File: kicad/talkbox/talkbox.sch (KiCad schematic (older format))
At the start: 40 parts, among them J1 AudioJack2, J2 Conn_01x02, J3 AudioJack2, J4 Barrel_Jack_Switch, SW1 SW_SPST, U1 LM386, U2 SW_3PDT, U3 TL071, U4 LT1054xSOIC16, U5 LM7812_TO220, U6 LM7912_TO220

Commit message: Added gitignore
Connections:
- net tone_control_output: now also R1.1, RV3.3
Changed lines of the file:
@@
 	3800 4850 4900 4850
 Wire Wire Line
-	6000 5950 6000 4750
-Wire Wire Line
-	4950 5950 6000 5950
+	6500 5950 6500 4750
+Wire Wire Line
+	4950 5950 6500 5950
 Text GLabel 5100 5350 3    50   Input ~ 0
 VDD
@@
 	5100 4050 5100 4250
 Connection ~ 5100 4250
-Text GLabel 6300 4750 2    50   Input ~ 0
+Text GLabel 6800 4750 2    50   Input ~ 0
 tone_control_output
 Wire Wire Line
-	6300 4750 6000 4750
+	6800 4750 6500 4750
 Wire Notes Line width 39 style dash_dot rgb(132, 132, 132)
 	7700 7050 7700 900
@@
 	13450 2200 13600 2200
 Wire Wire Line
-	5500 4750 6000 4750
-Connection ~ 6000 4750
+	5500 4750 6500 4750
+Connection ~ 6500 4750
 NoConn ~ 6500 9150
 NoConn ~ 6350 7850
@@
 Wire Wire Line
 	2900 8250 2900 8350
+Wire Wire Line
+	6000 1900 6500 1900
+Connection ~ 6000 1900
+Wire Wire Line
+	6500 1900 6500 4750
 $EndSCHEMATC

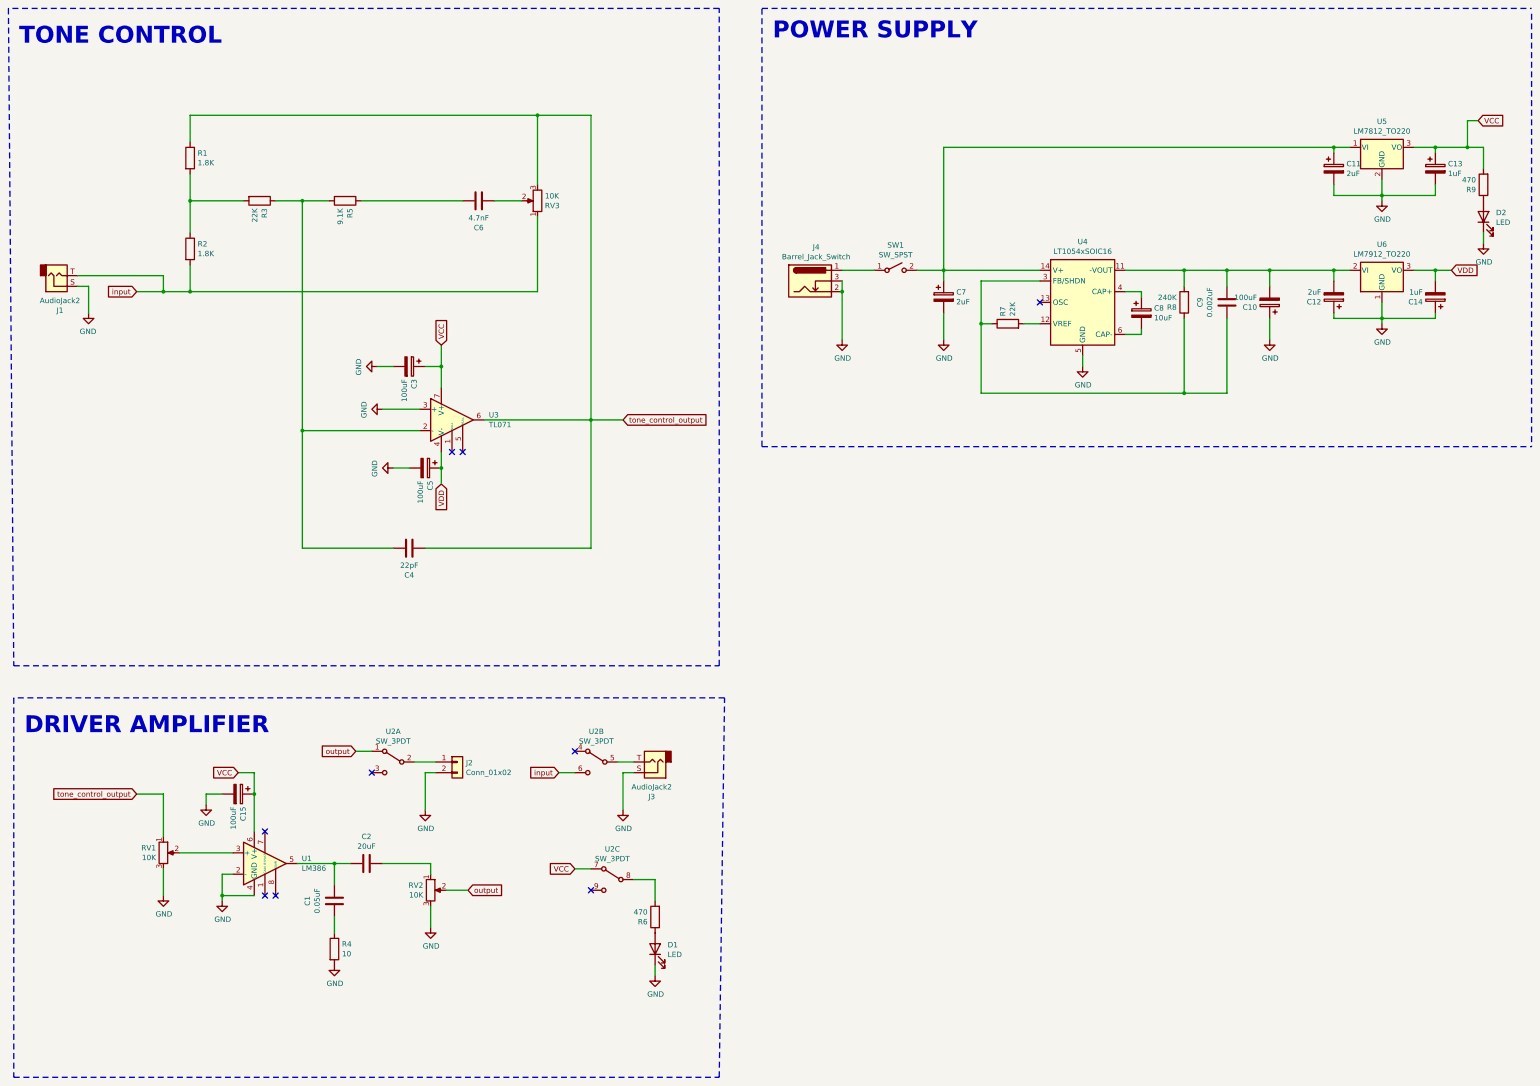
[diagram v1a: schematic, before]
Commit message: Added tl072 and preamp stage
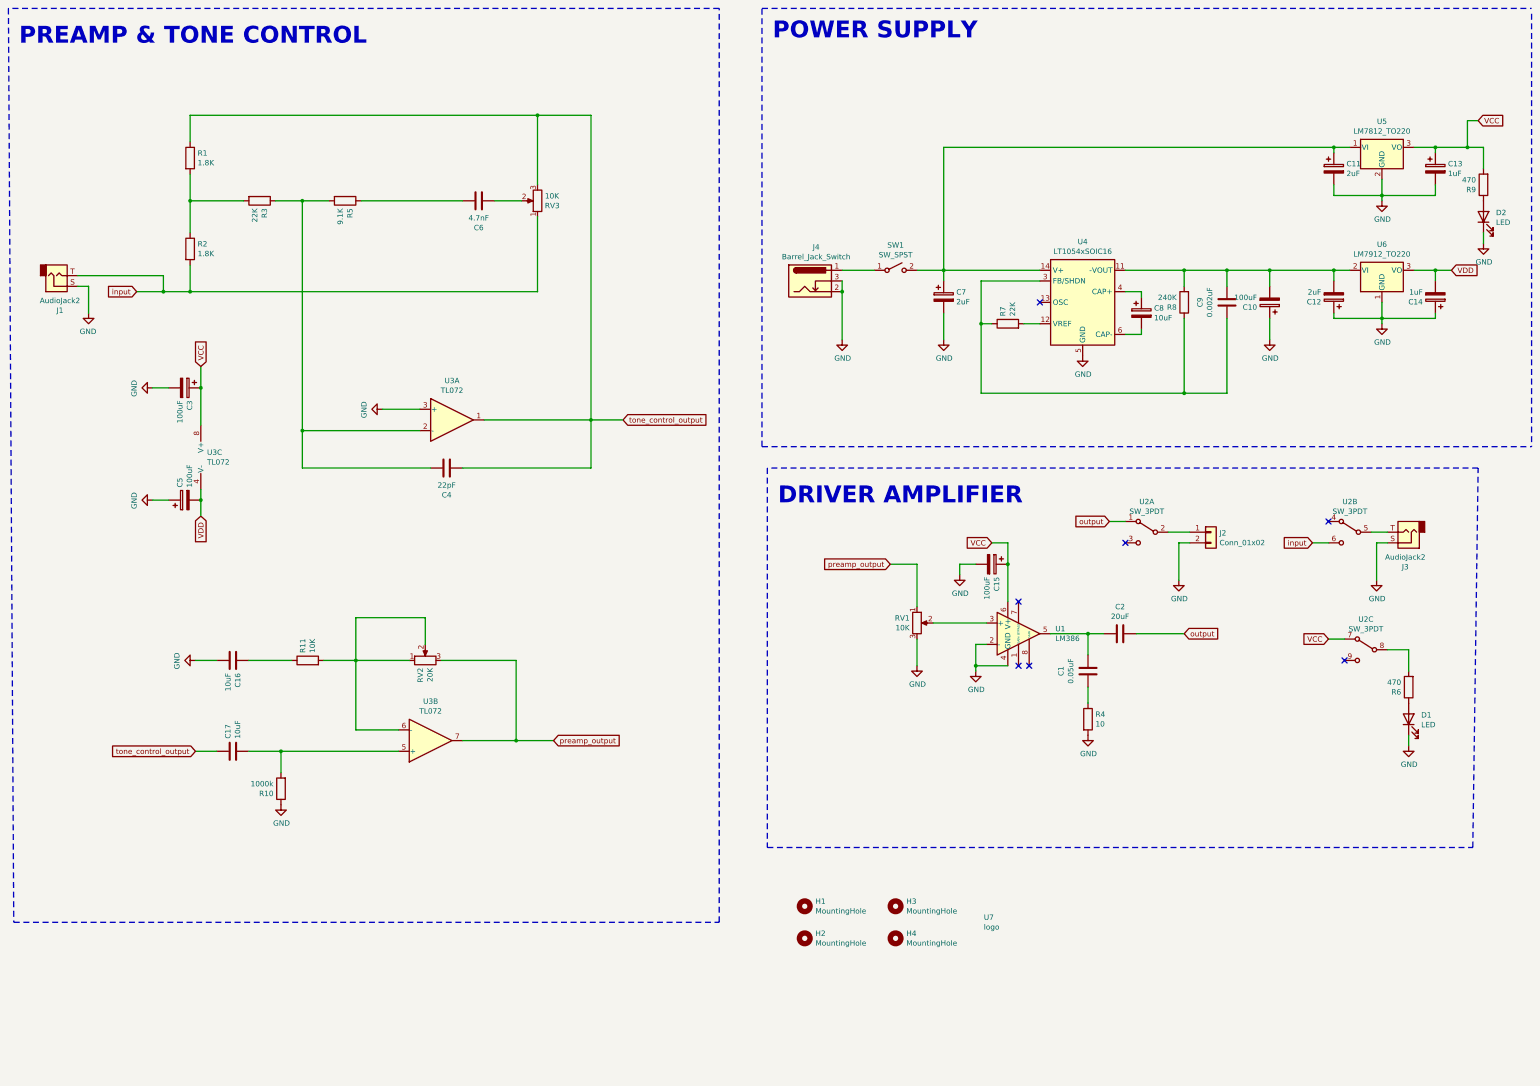
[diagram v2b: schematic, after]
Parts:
- removed U3: TL071, Package_SO:SOIC-8_3.9x4.9mm_P1.27mm, symbol Amplifier_Operational:TL071
- added C16, C17: 10uF, Capacitor_SMD:C_0603_1608Metric, symbol Device:C
- added H1, H2, H3, H4: MountingHole, MountingHole:MountingHole_3mm, symbol Mechanical:MountingHole
- added R10: 1000k, Resistor_SMD:R_0603_1608Metric, symbol Device:R
- added R11: 10K, Resistor_SMD:R_0603_1608Metric, symbol Device:R
- added U3: TL072, Package_SO:SOIC-8_3.9x4.9mm_P1.27mm, symbol Amplifier_Operational:TL072
- added U7: logo, imgs:ratatech_bitmap_10x2.8mm, symbol logo:logo
- RV2: value 10K -> 20K
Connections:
- net GND: now also C5.1, C16.2, R10.1, U3.3 (+); no longer C5.2, RV2.3
- net VCC: now also U3.8 (V+)
- net VDD: now also C5.2, U3.4 (V-); no longer C5.1
- net output: now also C2.1; no longer RV2.2
- net tone_control_output: now also C17.1, U3.1; no longer RV1.1
- net at C4.1, R3.1, R5.2: now also U3.2 (-)
- net at RV2.1: now also RV2.2, R11.2, U3.6 (-); no longer C2.1
- new net: C17.2, R10.2, U3.5 (+)
- new net: C16.1, R11.1
- new net preamp_output: RV1.1, RV2.3, U3.7
- no-connect marks 9 -> 7
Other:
- note added: "PREAMP & TONE CONTROL"
- note removed: "TONE CONTROL"
- moved on the sheet: C1, C15, C2, C3, C4, C5, D1, J2, J3, R4, R6, RV1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

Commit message: Removed lm386 based power amplifier and adapted tone control
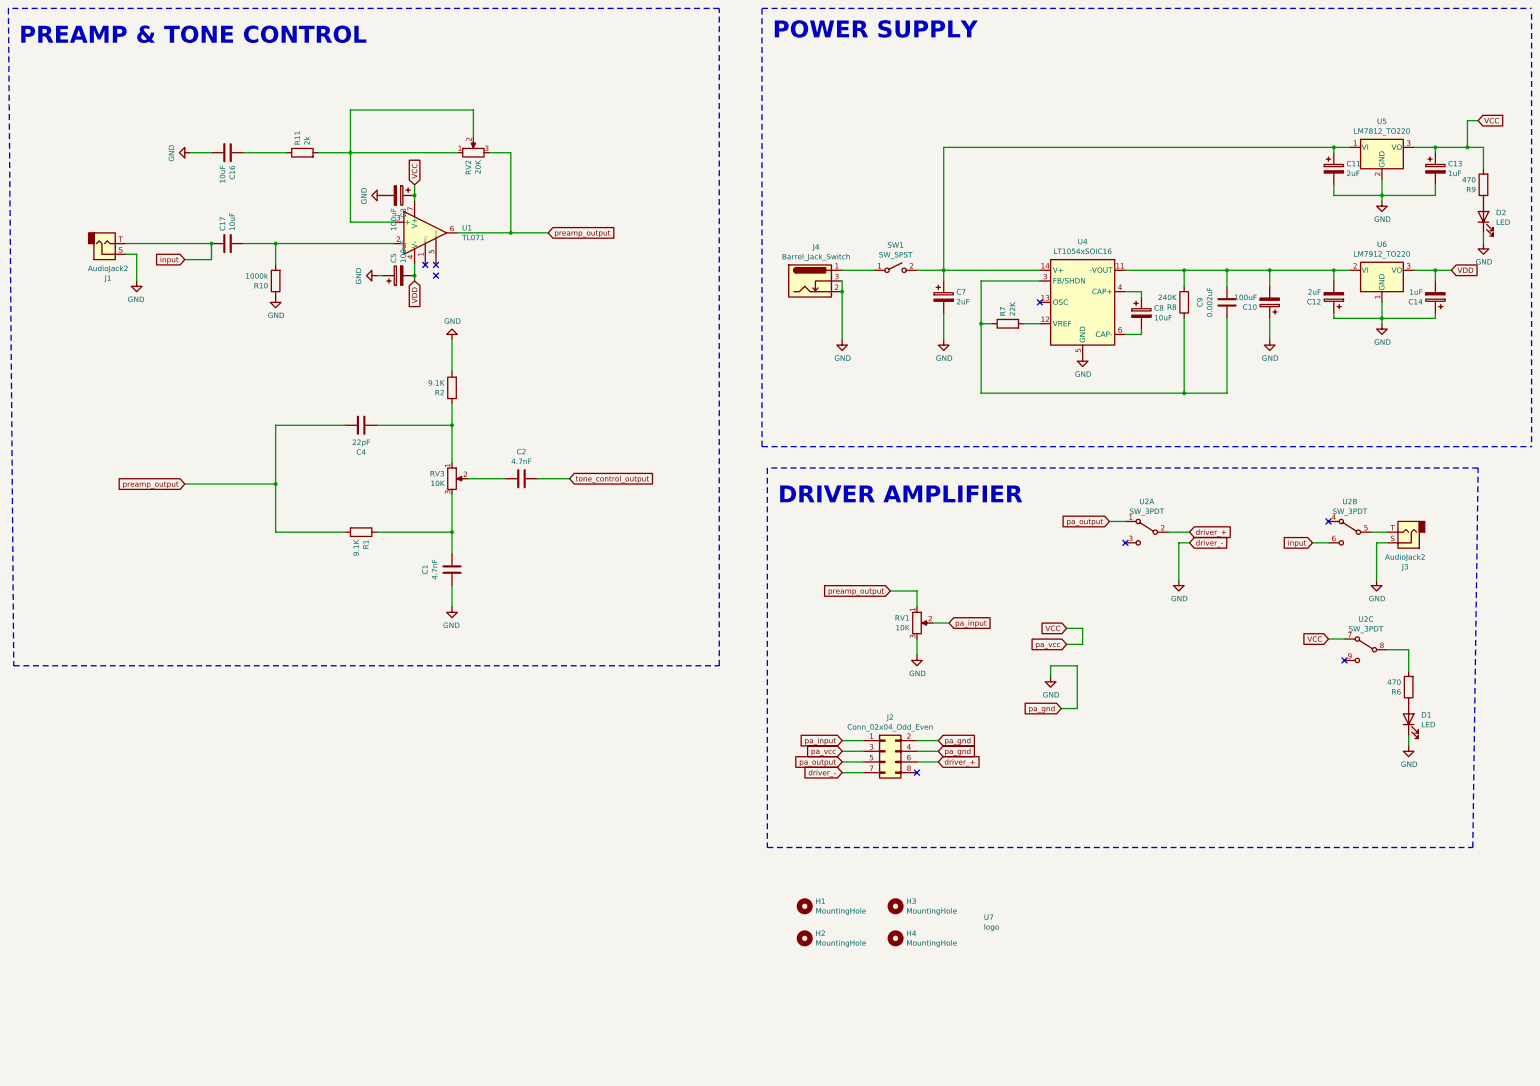
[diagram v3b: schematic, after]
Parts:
- removed C15: 100uF, Capacitor_SMD:CP_Elec_5x5.3, symbol Device:CP
- removed C6: 4.7nF, Capacitor_SMD:C_0603_1608Metric, symbol Device:C
- removed J2: Conn_01x02, Connector_JST:JST_EH_S2B-EH_1x02_P2.50mm_Horizontal, symbol Connector_Generic:Conn_01x02
- removed R3: 22K, Resistor_SMD:R_0603_1608Metric, symbol Device:R
- removed R4: 10, Resistor_SMD:R_0603_1608Metric, symbol Device:R
- removed R5: 9.1K, Resistor_SMD:R_0603_1608Metric, symbol Device:R
- removed U1: LM386, Package_SO:SOIC-8_3.9x4.9mm_P1.27mm, symbol Amplifier_Audio:LM386
- removed U3: TL072, Package_SO:SOIC-8_3.9x4.9mm_P1.27mm, symbol Amplifier_Operational:TL072
- added J2: Conn_02x04_Odd_Even, Connector_PinHeader_2.54mm:PinHeader_2x04_P2.54mm_Vertical, symbol Connector_Generic:Conn_02x04_Odd_Even
- added U1: TL071, Package_SO:SOIC-8_3.9x4.9mm_P1.27mm, symbol Amplifier_Operational:TL071
- C1: value 0.05uF -> 4.7nF
- C2: value 20uF -> 4.7nF; footprint Capacitor_SMD:CP_Elec_5x5.3 -> Capacitor_SMD:C_0603_1608Metric
- R1, R2: value 1.8K -> 9.1K
- R11: value 10K -> 2k
- U2: footprint Stompbox_Switch:SW_Stompbox_3PDT_redux -> Connector_PinHeader_2.54mm:PinHeader_2x05_P2.54mm_Vertical
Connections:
- net GND: now also C1.2, R2.2, J2.2 (Pin_2), J2.4 (Pin_4), J2.7 (Pin_7)
- net VCC: now also J2.3 (Pin_3), U1.7 (V+)
- net VDD: now also U1.4 (V-)
- net input: now also C17.1; no longer R2.2, RV3.1
- net preamp_output: now also C4.1, R1.2, U1.6
- net tone_control_output: now also C2.1; no longer C17.1, C4.2, R1.1, RV3.3
- net pa_input: now reaches RV1.2
- net pa_input: now also J2.1 (Pin_1)
- net at C1.1: now also R1.1, RV3.3; no longer C2.2
- net at C17.2, R10.2: now also U1.2 (-)
- net at R11.2, RV2.1, RV2.2: now also U1.3 (+)
- net at RV3.2: now also C2.2
- net at R2.1: now also C4.2, RV3.1; no longer R1.2
- net driver_+: now reaches U2.2 (B)
- net driver_+: now also J2.6 (Pin_6)
- net output renamed pa_output
- net pa_output: now also J2.5 (Pin_5); no longer C2.1
- no-connect marks 7 -> 8
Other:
- moved on the sheet: C16, C17, C3, C4, C5, J1, R10, R11, RV2

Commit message: Changed preamp capacitors to electrolytics
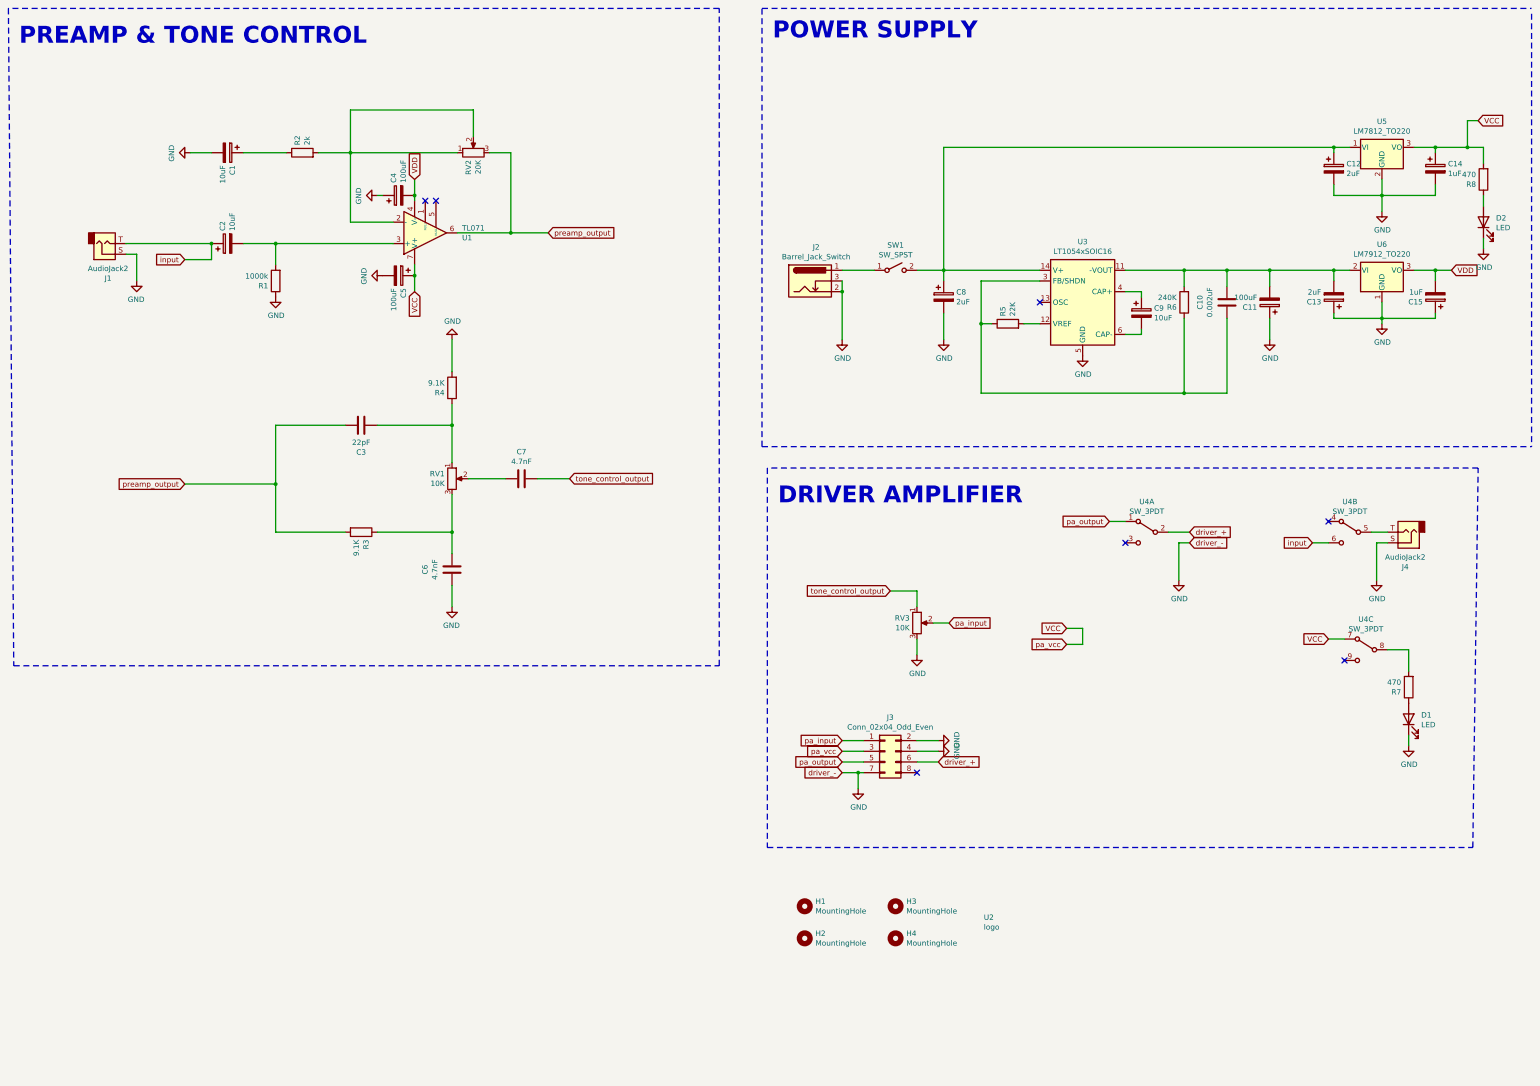
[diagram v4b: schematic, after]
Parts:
- removed C16, C17: 10uF, Capacitor_SMD:C_0603_1608Metric, symbol Device:C
- added C1, C2: 10uF, Capacitor_SMD:CP_Elec_5x5.3, symbol Device:CP
- renumbered C9 to C10, C10 to C11, C11 to C12, C12 to C13, C13 to C14, C14 to C15, C4 to C3, C5 to C4, C3 to C5, C1 to C6, C2 to C7, C7 to C8, C8 to C9, J4 to J2, J2 to J3, J3 to J4, R10 to R1, R11 to R2, R1 to R3, R2 to R4, R7 to R5, R8 to R6, R6 to R7, R9 to R8, RV3 to RV1, RV1 to RV3, U7 to U2, U4 to U3, U2 to U4
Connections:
- net GND: now also C1.2
- net input: now also C2.1
- net preamp_output: no longer RV3.1
- net tone_control_output: now also RV3.1
- net at R1.2: now also U1.3 (+), C2.2; no longer U1.2 (-)
- net at R2.1: now also C1.1
- net at R2.2, RV2.1, RV2.2: now also U1.2 (-); no longer U1.3 (+)
- no-connect marks 8 -> 7
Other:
- moved on the sheet: C4, C5, D2, R8
